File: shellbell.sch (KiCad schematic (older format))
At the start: 23 parts, among them J1 Barrel_Jack_MountingPin, J2 Conn_02x04_Odd_Even, J3 USB_B_Mini, Q1 IRLB8721PBF, U1 LD1117V33, U2 FT230XS-U

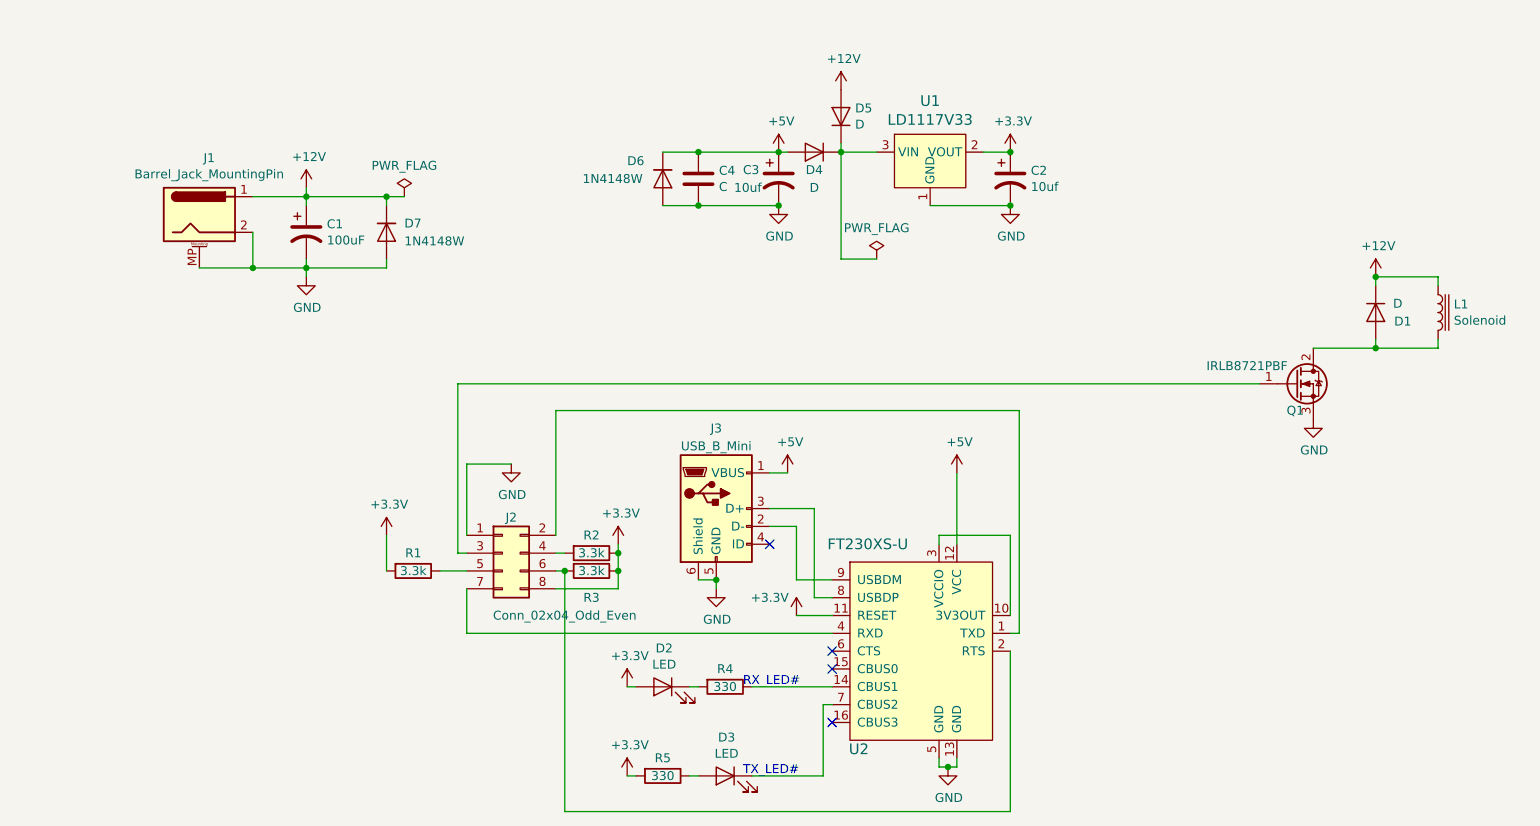
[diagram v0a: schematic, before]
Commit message: Fixes TX/RX. Removes RTS-reset. Clean up.
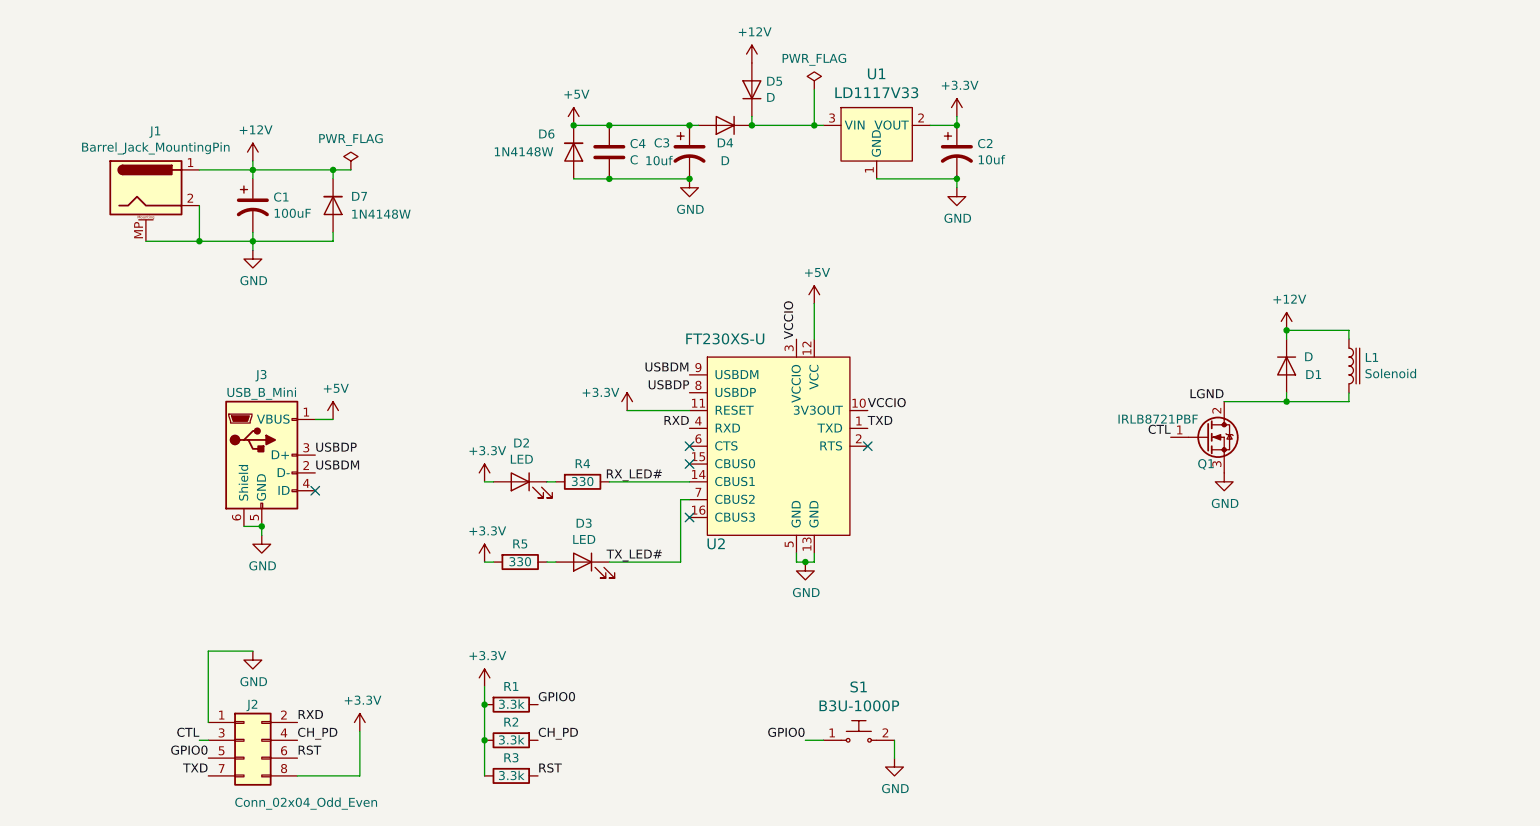
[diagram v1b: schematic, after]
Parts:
- added S1: B3U-1000P, digikey-footprints:Switch_Tactile_SMD_B3U-1000P, symbol dk_Tactile-Switches:B3U-1000P
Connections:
- net GND: now also S1.2
- net CTL: now reaches J2.3 (Pin_3), Q1.1 (G)
- net LGND: now reaches D1.2 (A), L1.2, Q1.2 (D)
- net RXD: now reaches J2.2 (Pin_2)
- net RXD: now also U2.4 (RXD); no longer U2.1 (TXD)
- net VCCIO: now reaches U2.10 (3V3OUT), U2.3 (VCCIO)
- net RX_LED#: now reaches R4.1, U2.14 (CBUS1)
- net RST: now reaches J2.6 (Pin_6), R3.2
- net RST: no longer U2.2 (RTS)
- net TXD: now reaches J2.7 (Pin_7)
- net TXD: now also U2.1 (TXD); no longer U2.4 (RXD)
- net TX_LED#: now reaches D3.1 (K), U2.7 (CBUS2)
- net USBDP: now reaches J3.3 (D+), U2.8 (USBDP)
- net USBDM: now reaches J3.2 (D-), U2.9 (USBDM)
- net CH_PD: now reaches J2.4 (Pin_4), R2.2
- net GPIO0: now reaches J2.5 (Pin_5), R1.1
- net GPIO0: now also S1.1
- no-connect marks 4 -> 5
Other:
- note removed: "RX_LED#"
- note removed: "TX_LED#"
- moved on the sheet: C1, C2, C3, C4, D1, D2, D3, D4, D5, D6, D7, J1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

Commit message: Add programming buttons and rerouting.
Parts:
- removed S1: B3U-1000P, digikey-footprints:Switch_Tactile_SMD_B3U-1000P, symbol dk_Tactile-Switches:B3U-1000P
- added H1: MountingHole_Pad, MountingHole:MountingHole_2.2mm_M2_Pad_Via, symbol Mechanical:MountingHole_Pad
- added S2: GPIO0, B3U-3000P:SW_B3U-3000P, symbol B3U-3000P:B3U-3000P
- added S3: RST, B3U-3000P:SW_B3U-3000P, symbol B3U-3000P:B3U-3000P
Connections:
- net GND: now also H1.1, S2.2, S3.2
- net GPIO0: now also S2.1
- net RST: now also S3.1
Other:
- moved on the sheet: C1, C2, C3, C4, D1, D2, D3, D4, D5, D6, D7, J1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
